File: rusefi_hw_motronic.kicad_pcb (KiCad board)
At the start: 2 copper layers, 175 x 129 mm, 50 parts, among them J1 OMEGA PCC_SMP_K, J2 Conn_01x02_Female, Q1 Q_NIGBT_CEG, Q2 Q_NIGBT_CEG, Q3 Q_NIGBT_CEG, U1 SFH617A-2X009T, U2 BOSCH_55P, U3 molex_48pin_MRE, U4 MAX31855KASA, U5 TPIC8101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

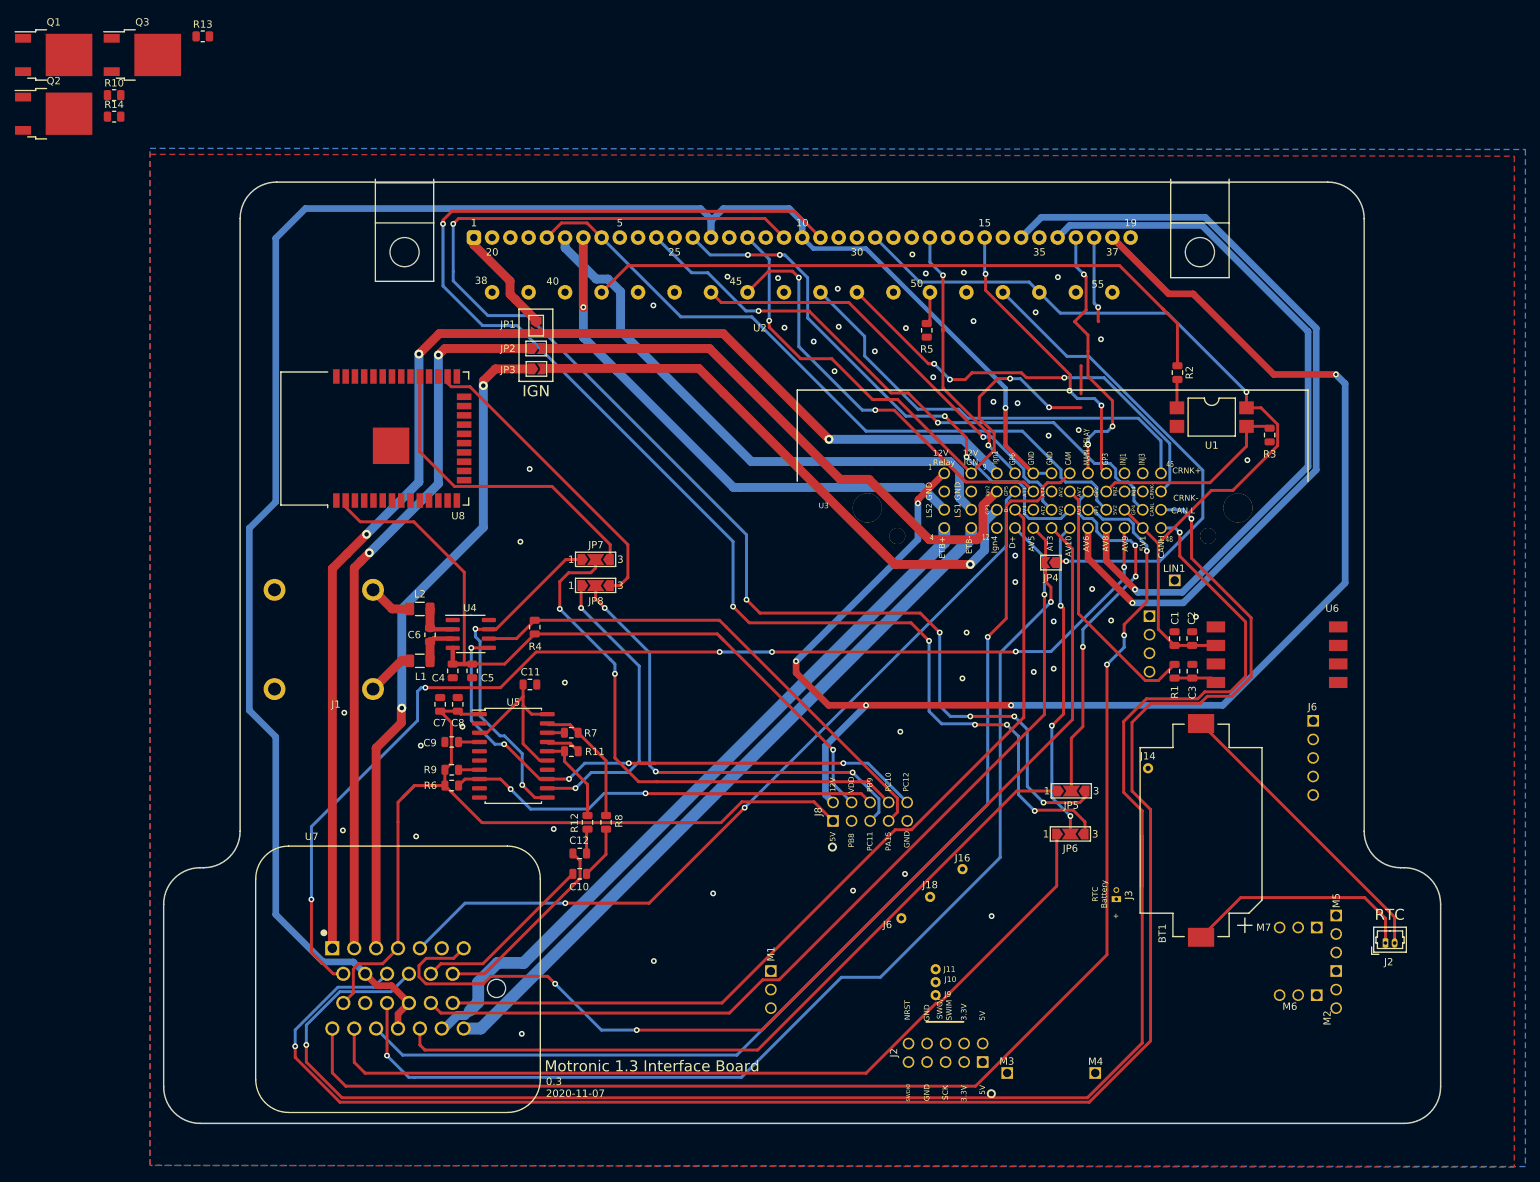
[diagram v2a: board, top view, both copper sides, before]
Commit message: routed ignitors
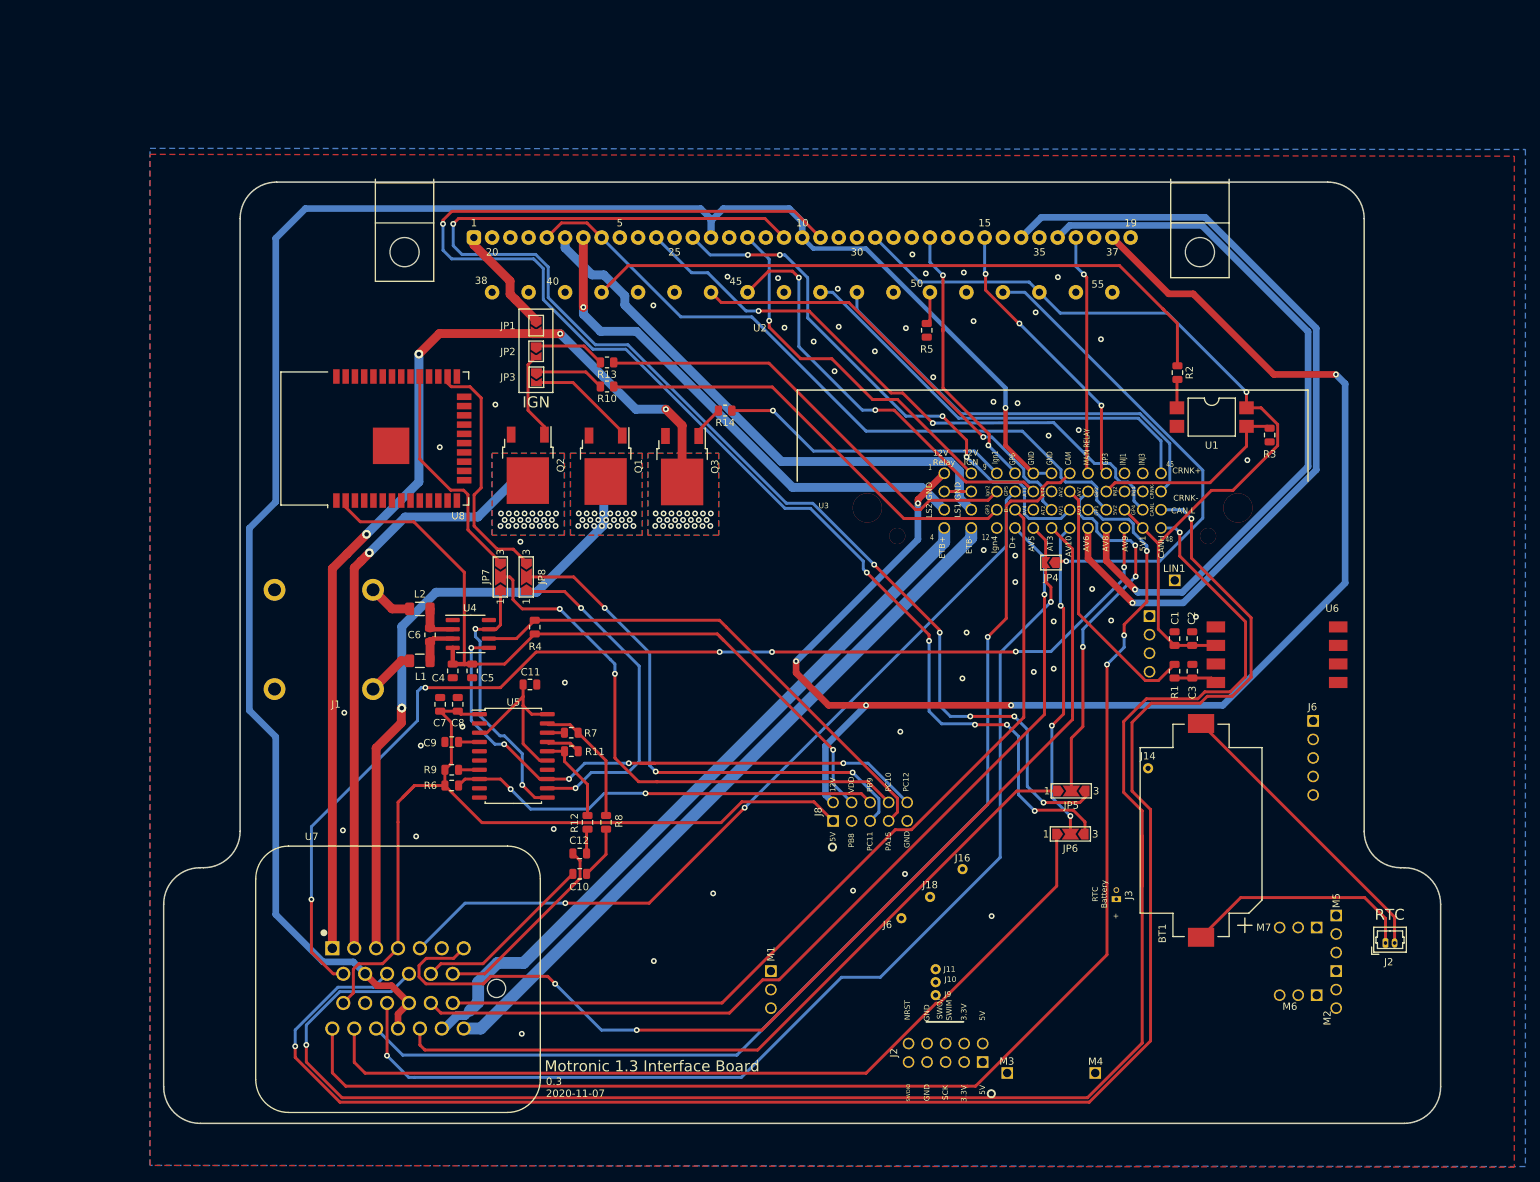
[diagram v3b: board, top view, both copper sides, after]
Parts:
- moved Q1 94.3 mm to (83.8, 66.7), turned to 270 degrees
- moved Q3 93.0 mm to (94.2, 66.7), turned to 270 degrees
- moved R14 92.9 mm to (100.1, 59.1), turned to 180 degrees
- moved Q2 80.9 mm to (73.1, 66.5), turned to 270 degrees
- moved R10 78.5 mm to (83.9, 55.8), turned to 180 degrees
- moved R13 71.2 mm to (83.9, 52.5), turned to 180 degrees
- moved JP7 13.3 mm to (69.3, 81.9), turned to 90 degrees
- moved JP8 9.56 mm to (72.9, 81.9), turned to 90 degrees
- moved JP3 1.14 mm to (74.3, 54.5), turned to 270 degrees
- moved JP2 0.38 mm to (74.2, 50.9), turned to 270 degrees
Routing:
- net IGN_A: track 0.00 -> 39.9 mm, vias 0 -> 1
- net IGN1: track 174.6 -> 137.2 mm, vias 3 -> 27
- net IGN_SWITCH: track 78.7 -> 49.5 mm, vias 3 -> 1
- net IGN2: track 99.1 -> 79.8 mm, vias 2 -> 24
- net IGN_C: track 78.6 -> 60.5 mm, vias 1 -> 0
- net IGN_B: track 77.9 -> 61.9 mm
- net Net-(JP3-Pad2): track 0.00 -> 15.1 mm
- net TS_WIFI_TX: track 43.7 -> 31.1 mm
- net Net-(JP2-Pad2): track 0.00 -> 12.1 mm
- net +BATT: track 11.8 -> 0.00 mm, vias 1 -> 0
- net MISO: track 47.0 -> 36.8 mm
- net Net-(JP2-Pad1): track 0.00 -> 9.73 mm
- net Net-(JP3-Pad1): track 0.00 -> 9.59 mm
- net PC11: track 64.6 -> 73.5 mm
- net TS_WIFI_RX: track 42.2 -> 33.5 mm
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- added copper zone on B.Cu, net IGN1
- added copper zone on F.Cu, net IGN1
- added copper zone on B.Cu, net IGN2
- added copper zone on F.Cu, net IGN2
- added copper zone on B.Cu, net IGN3
- added copper zone on F.Cu, net IGN3

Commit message: more routing, getting closer to fab
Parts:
- removed U6: MPXA4250A6U, rusefi_hw_motronic:MPXA4250A6U
- added C13: 0.1uF, Capacitor_SMD:C_0805_2012Metric, F.Cu at (59.7, 75.4)
- added C14: 0.1uF, Capacitor_SMD:C_0805_2012Metric, F.Cu at (53.1, 75.4)
- added C15: 10uF, Capacitor_SMD:C_0805_2012Metric, F.Cu at (55.4, 75.4)
- added D1: LED, LED_SMD:LED_0603_1608Metric, F.Cu at (62.7, 51.8)
- added J3: Conn_01x03_Male, Connector_PinSocket_1.27mm:PinSocket_1x03_P1.27mm_Vertical_SMD_Pin1Left, F.Cu at (51.1, 47.1)
- added R15: 10K, Resistor_SMD:R_0805_2012Metric, F.Cu at (62.0, 75.3)
- added R16: 220, Resistor_SMD:R_0805_2012Metric, F.Cu at (66.4, 51.8)
- added U9: MPXA6400A, rusefi_hw_motronic:MPXA4250A6U, F.Cu at (184.2, 88.6)
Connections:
- U8 pad 34: Net-(U8-Pad34) -> RX
- U8 pad 35: Net-(U8-Pad35) -> TX
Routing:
- net Net-(R16-Pad1): track 0.00 -> 19.7 mm, vias 0 -> 2
- net CAN_H: track 239.3 -> 221.4 mm
- net Net-(C13-Pad1): track 0.00 -> 17.4 mm
- net SENSOR_GND: track 258.1 -> 247.2 mm
- net CAN_L: track 236.2 -> 225.6 mm
- net RX: track 0.00 -> 9.03 mm
- net PPS1: track 189.5 -> 197.5 mm
- net RTC_BATT+: track 32.1 -> 25.6 mm
- net TX: track 0.00 -> 6.33 mm
- net TPS1: track 154.0 -> 150.9 mm
- net +3V3: track 105.2 -> 107.5 mm
- net Net-(D1-Pad2): track 0.00 -> 1.98 mm
- net USB-: track 123.4 -> 125.3 mm
- net BARO: track 35.3 -> 33.4 mm
- net PPS2: track 119.3 -> 118.7 mm
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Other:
- board text added: "0.4 2021-01-15"
- board text removed: "0.3 2020-11-07"

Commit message: fab v0.4
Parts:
- added C16: 0.1uF, Capacitor_SMD:C_0805_2012Metric, F.Cu at (55.4, 51.6)
- added G***: LOGO, rusefi_motronic:rusefi_logo, F.Cu at (98.6, 125.0)
- added R17: 10K, Resistor_SMD:R_0805_2012Metric, F.Cu at (55.4, 49.5)
- added SW1: RESET, Button_Switch_SMD:SW_Push_SPST_NO_Alps_SKRK, F.Cu at (61.0, 81.8)
- added SW2: BOOT, Button_Switch_SMD:SW_Push_SPST_NO_Alps_SKRK, F.Cu at (56.4, 46.7)
- R16: value 220 -> 100
- moved J3 2.39 mm to (48.8, 47.8)
- moved C11 1.45 mm to (73.4, 98.0)
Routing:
- net +3V3: track 107.5 -> 132.6 mm, vias 1 -> 3
- net Net-(C13-Pad1): track 17.4 -> 40.3 mm, vias 0 -> 2
- net Net-(C16-Pad1): track 0.00 -> 14.4 mm
- net +5V: track 235.5 -> 228.6 mm
- net Net-(C11-Pad1): track 24.2 -> 22.6 mm
- net TX: track 6.33 -> 7.10 mm

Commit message: fixed gnd issues
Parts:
- renumbered SW2 to BOOT, SW1 to RST
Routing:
- net GND: vias 57 -> 70
